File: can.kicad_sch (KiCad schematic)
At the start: 12 parts, among them U7 MCP251863, Y1 40MHz

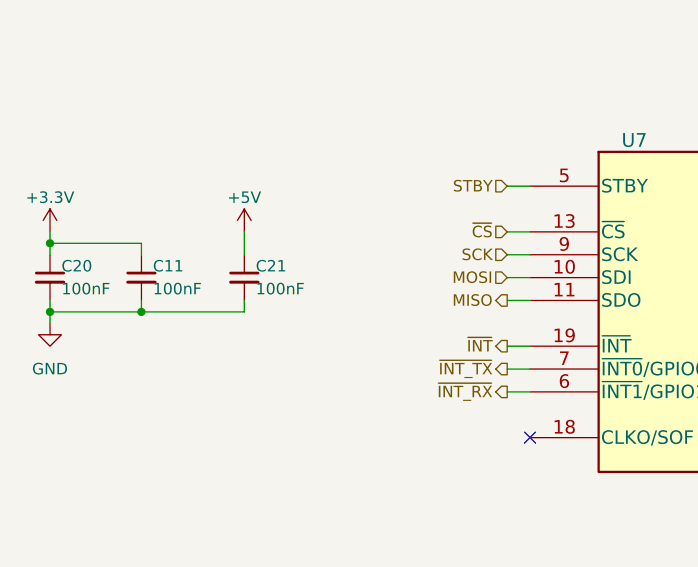
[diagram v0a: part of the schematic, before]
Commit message: Finish connecting everything in sch.
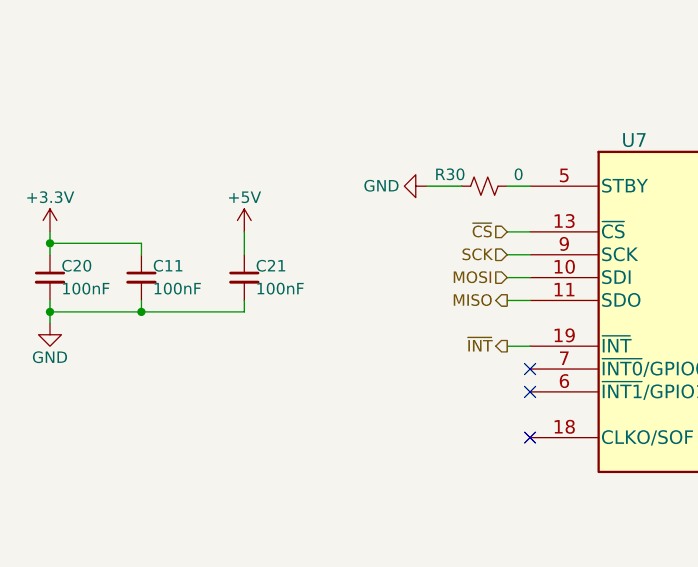
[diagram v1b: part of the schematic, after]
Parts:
- added R30: 0, symbol Device:R_Small_US
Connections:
- net GND: now also R30.1
- net STBY: no longer names the net of U7.5 (STBY)
- net STBY: now also R30.2
- net ~{INT_RX}: no longer names the net of U7.6 (~{INT1}/GPIO1/XSTBY)
- net ~{INT_TX}: no longer names the net of U7.7 (~{INT0}/GPIO0)
- no-connect marks 1 -> 3
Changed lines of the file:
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@@
   (junction (at 190.5 74.93) (diameter 0) (color 0 0 0 0)
   )
+  (no_connect (at 119.38 90.17))
+  (no_connect (at 119.38 87.63))
   (no_connect (at 119.38 95.25))
   (wire (pts (xy 191.77 96.52) (xy 191.77 99.06))
@@
     (stroke (width 0) (type default))
   )
+  (wire (pts (xy 107.95 67.31) (xy 111.76 67.31))
+    (stroke (width 0) (type default))
+  )
   (wire (pts (xy 236.22 68.58) (xy 236.22 69.85))
     (stroke (width 0) (type default))
@@
     (stroke (width 0) (type default))
   )
-  (wire (pts (xy 116.84 90.17) (xy 119.38 90.17))
-    (stroke (width 0) (type default))
-  )
   (wire (pts (xy 66.04 73.66) (xy 66.04 74.93))
     (stroke (width 0) (type default))
@@
   )
   (wire (pts (xy 116.84 85.09) (xy 119.38 85.09))
-    (stroke (width 0) (type default))
-  )
-  (wire (pts (xy 116.84 87.63) (xy 119.38 87.63))
     (stroke (width 0) (type default))
   )
@@
     (effects (font (size 1.27 1.27)) (justify left))
   )
-  (hierarchical_label "~{INT_RX}" (shape output) (at 116.84 90.17 180) (fields_autoplaced)
-    (effects (font (size 1.27 1.27)) (justify right))
-  )
   (hierarchical_label "CAN_L" (shape bidirectional) (at 248.92 74.93 0) (fields_autoplaced)
     (effects (font (size 1.27 1.27)) (justify left))
@@
     (effects (font (size 1.27 1.27)) (justify right))
   )
-  (hierarchical_label "~{INT_TX}" (shape output) (at 116.84 87.63 180) (fields_autoplaced)
-    (effects (font (size 1.27 1.27)) (justify right))
-  )
   (hierarchical_label "SCK" (shape input) (at 116.84 74.93 180) (fields_autoplaced)
     (effects (font (size 1.27 1.27)) (justify right))
   )
   (hierarchical_label "MOSI" (shape input) (at 116.84 77.47 180) (fields_autoplaced)
-    (effects (font (size 1.27 1.27)) (justify right))
-  )
-  (hierarchical_label "STBY" (shape input) (at 116.84 67.31 180) (fields_autoplaced)
     (effects (font (size 1.27 1.27)) (justify right))
   )
@@
     )
   )
+  (symbol (lib_id "Device:R_Small_US") (at 114.3 67.31 90) (unit 1)
+    (in_bom yes) (on_board yes) (dnp no)
+    (property "Reference" "R30" (at 110.49 66.04 90)
+      (effects (font (size 1.27 1.27)))
+    )
+    (property "Value" "0" (at 118.11 66.04 90)
+      (effects (font (size 1.27 1.27)))
+    )
+    (property "Footprint" "" (at 114.3 67.31 0)
+      (effects (font (size 1.27 1.27)) hide)
+    )
+    (property "Datasheet" "~" (at 114.3 67.31 0)
+      (effects (font (size 1.27 1.27)) hide)
+    )
+    (pin "1")
+    (pin "2")
+    (instances
+      (project "main-board"
+        (path "/5ad67b7d-c56f-4b00-8953-cc84f90f9708/72ca2a69-64d2-4325-ac9e-ca976eb5a207"
+          (reference "R30") (unit 1)
+        )
+      )
+    )
+  )
   (symbol (lib_id "power:+5V") (at 87.63 72.39 0) (unit 1)
     (in_bom yes) (on_board yes) (dnp no) (fields_autoplaced)
@@
     )
   )
+  (symbol (lib_id "power:GND") (at 107.95 67.31 270) (unit 1)
+    (in_bom yes) (on_board yes) (dnp no)
+    (property "Reference" "#PWR065" (at 101.6 67.31 0)
+      (effects (font (size 1.27 1.27)) hide)
+    )
+    (property "Value" "GND" (at 102.87 67.31 90)
+      (effects (font (size 1.27 1.27)))
+    )
+    (property "Footprint" "" (at 107.95 67.31 0)
+      (effects (font (size 1.27 1.27)) hide)
+    )
+    (property "Datasheet" "" (at 107.95 67.31 0)
+      (effects (font (size 1.27 1.27)) hide)
+    )
+    (pin "1")
+    (instances
+      (project "main-board"
+        (path "/5ad67b7d-c56f-4b00-8953-cc84f90f9708/72ca2a69-64d2-4325-ac9e-ca976eb5a207"
+          (reference "#PWR065") (unit 1)
+        )
+      )
+    )
+  )
   (symbol (lib_id "Device:Crystal_GND24_Small") (at 191.77 93.98 90) (unit 1)
     (in_bom yes) (on_board yes) (dnp no)
@@
   )
   (symbol (lib_id "power:GND") (at 66.04 82.55 0) (unit 1)
-    (in_bom yes) (on_board yes) (dnp no) (fields_autoplaced)
+    (in_bom yes) (on_board yes) (dnp no)
     (property "Reference" "#PWR048" (at 66.04 88.9 0)
       (effects (font (size 1.27 1.27)) hide)
     )
-    (property "Value" "GND" (at 66.04 87.63 0)
-      (effects (font (size 1.27 1.27)))
-    )
+    (property "Value" "GND" (at 66.04 86.36 0)
+      (effects (font (size 1.27 1.27)))
+    )

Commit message: Assign some of the footprints and MPNs.
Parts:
- C11, C20, C21, C22, C23, C24, C25, C26: footprint (none) -> Capacitor_SMD:C_0402_1005Metric
- R21, R22, R30: footprint (none) -> Resistor_SMD:R_0402_1005Metric
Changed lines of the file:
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@@
       (effects (font (size 1.27 1.27)))
     )
-    (property "Footprint" "" (at 114.3 67.31 0)
+    (property "Footprint" "Resistor_SMD:R_0402_1005Metric" (at 114.3 67.31 0)
       (effects (font (size 1.27 1.27)) hide)
     )
@@
       (effects (font (size 1.27 1.27)) (justify left))
     )
-    (property "Footprint" "" (at 76.2 77.47 0)
+    (property "Footprint" "Capacitor_SMD:C_0402_1005Metric" (at 76.2 77.47 0)
       (effects (font (size 1.27 1.27)) hide)
     )
@@
       (effects (font (size 1.27 1.27)))
     )
-    (property "Footprint" "" (at 199.39 99.06 0)
+    (property "Footprint" "Capacitor_SMD:C_0402_1005Metric" (at 199.39 99.06 0)
       (effects (font (size 1.27 1.27)) hide)
     )
@@
       (effects (font (size 1.27 1.27)))
     )
-    (property "Footprint" "" (at 210.82 68.58 0)
+    (property "Footprint" "Capacitor_SMD:C_0402_1005Metric" (at 210.82 68.58 0)
       (effects (font (size 1.27 1.27)) hide)
     )
@@
       (effects (font (size 1.27 1.27)))
     )
-    (property "Footprint" "" (at 196.85 66.04 0)
+    (property "Footprint" "Resistor_SMD:R_0402_1005Metric" (at 196.85 66.04 0)
       (effects (font (size 1.27 1.27)) hide)
     )
@@
       (effects (font (size 1.27 1.27)))
     )
-    (property "Footprint" "" (at 236.22 72.39 0)
+    (property "Footprint" "Capacitor_SMD:C_0402_1005Metric" (at 236.22 72.39 0)
       (effects (font (size 1.27 1.27)) hide)
     )
@@
       (effects (font (size 1.27 1.27)))
     )
-    (property "Footprint" "" (at 196.85 71.12 0)
+    (property "Footprint" "Resistor_SMD:R_0402_1005Metric" (at 196.85 71.12 0)
       (effects (font (size 1.27 1.27)) hide)
     )
@@
       (effects (font (size 1.27 1.27)) (justify left))
     )
-    (property "Footprint" "" (at 87.63 77.47 0)
+    (property "Footprint" "Capacitor_SMD:C_0402_1005Metric" (at 87.63 77.47 0)
       (effects (font (size 1.27 1.27)) hide)
     )
@@
       (effects (font (size 1.27 1.27)))
     )
-    (property "Footprint" "" (at 199.39 88.9 0)
+    (property "Footprint" "Capacitor_SMD:C_0402_1005Metric" (at 199.39 88.9 0)
       (effects (font (size 1.27 1.27)) hide)
     )
@@
       (effects (font (size 1.27 1.27)) (justify left))
     )
-    (property "Footprint" "" (at 66.04 77.47 0)
+    (property "Footprint" "Capacitor_SMD:C_0402_1005Metric" (at 66.04 77.47 0)
       (effects (font (size 1.27 1.27)) hide)
     )
@@
       (effects (font (size 1.27 1.27)))
     )
-    (property "Footprint" "" (at 236.22 64.77 0)
-      (effects (font (size 1.27 1.27)) hide)
-    )
+    (property "Footprint" "Capacitor_SMD:C_0402_1005Metric" (at 236.22 64.77 0)
+      (effects (font (size 1.27 1.27)) hide)
+    )

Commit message: Import the previous main board to match the overall shape, and re-annotate the schematic.
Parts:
- C401: renamed from C25; footprint Capacitor_SMD:C_0402_1005Metric -> Capacitor_SMD:C_0603_1608Metric
- C402: renamed from C24; footprint Capacitor_SMD:C_0402_1005Metric -> Capacitor_SMD:C_0603_1608Metric
- C403: renamed from C26; footprint Capacitor_SMD:C_0402_1005Metric -> Capacitor_SMD:C_0603_1608Metric
- C404: renamed from C20; footprint Capacitor_SMD:C_0402_1005Metric -> Capacitor_SMD:C_0603_1608Metric; MPN (none) -> RM EMK105 B7104KV-F
- C405: renamed from C11; footprint Capacitor_SMD:C_0402_1005Metric -> Capacitor_SMD:C_0603_1608Metric; MPN (none) -> RM EMK105 B7104KV-F
- C406: renamed from C21; footprint Capacitor_SMD:C_0402_1005Metric -> Capacitor_SMD:C_0603_1608Metric; MPN (none) -> RM EMK105 B7104KV-F
- C407: renamed from C22; footprint Capacitor_SMD:C_0402_1005Metric -> Capacitor_SMD:C_0603_1608Metric
- C408: renamed from C23; footprint Capacitor_SMD:C_0402_1005Metric -> Capacitor_SMD:C_0603_1608Metric
- R401: renamed from R21; footprint Resistor_SMD:R_0402_1005Metric -> Resistor_SMD:R_0603_1608Metric
- R402: renamed from R30; footprint Resistor_SMD:R_0402_1005Metric -> Resistor_SMD:R_0603_1608Metric; MPN (none) -> RMCF0603ZT0R00
- R403: renamed from R22; footprint Resistor_SMD:R_0402_1005Metric -> Resistor_SMD:R_0603_1608Metric
- renumbered U7 to U401, Y1 to Y401

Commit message: Finish the draft routing.
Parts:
- removed C401, C402, C403: 4.7nF, Capacitor_SMD:C_0603_1608Metric, symbol Device:C_Small
- removed C404, C405, C406: 100nF, Capacitor_SMD:C_0603_1608Metric, symbol Device:C_Small
- removed C407, C408: 6pF, Capacitor_SMD:C_0603_1608Metric, symbol Device:C_Small
- removed R401, R403: 60.4, Resistor_SMD:R_0603_1608Metric, symbol Device:R_Small_US
- removed R402: 0, Resistor_SMD:R_0603_1608Metric, symbol Device:R_Small_US
- removed U401: MCP251863, Package_SO:SSOP-28_5.3x10.2mm_P0.65mm, symbol MCP251863:MCP251863
- removed Y401: 40MHz, Crystal:Crystal_SMD_2016-4Pin_2.0x1.6mm, symbol Device:Crystal_GND24_Small
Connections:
- no-connect marks 3 -> 0
